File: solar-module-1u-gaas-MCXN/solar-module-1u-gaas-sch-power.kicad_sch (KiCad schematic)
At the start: 53 parts, among them Q1 NTR4101P, Q2 DMP2240UDM-7, U10 TPS63060DSCR, U12 LTC4412, U3 LT1618EMSTRPBF, U4 INA226

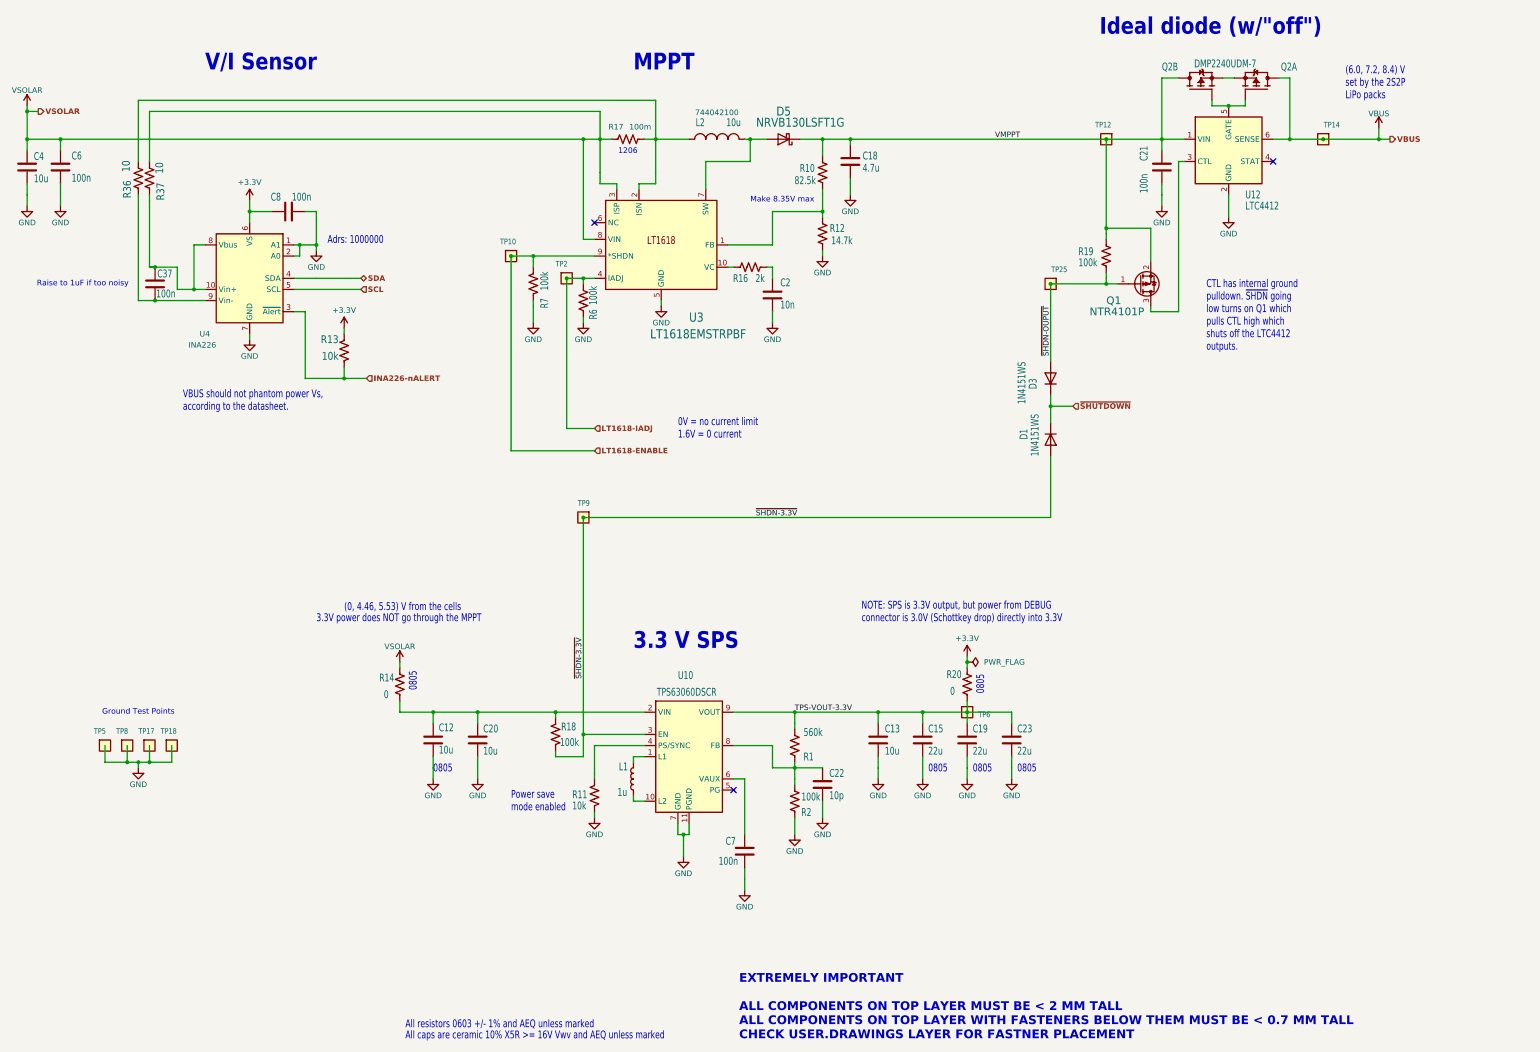
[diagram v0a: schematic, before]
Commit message: Solar Module with GaAs Cells and MCXN processor v1.1
Fixed BOM, fixed solar connector sync between brd/sch, routed UART lines to the connector, untented vias for venting. Sent to fab.
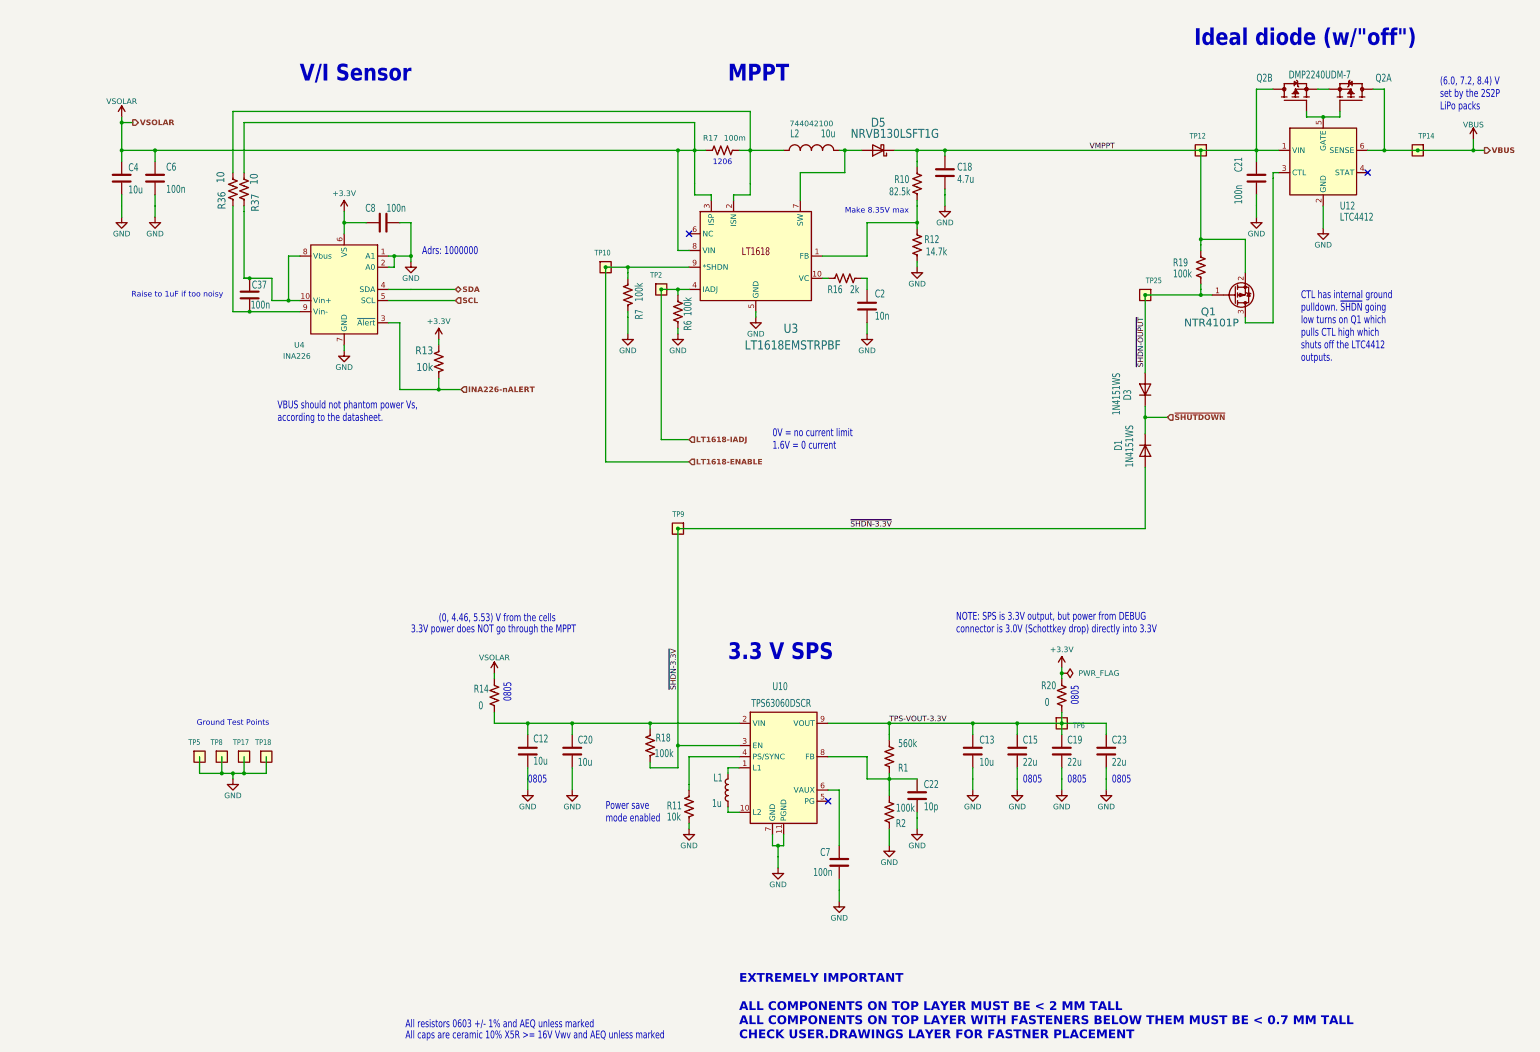
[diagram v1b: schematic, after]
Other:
- moved on the sheet: C12, C13, C15, C18, C19, C2, C20, C21, C22, C23, C37, C4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
